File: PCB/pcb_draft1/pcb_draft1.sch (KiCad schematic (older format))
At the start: 63 parts, among them Q1 DMN6140L, Q10 DMN6140L, Q11 DMN6140L, Q12 DMN6140L, Q13 DMN6140L, Q14 DMN6140L, Q15 DMN6140L, Q2 DMN6140L, Q3 DMN6140L, Q4 DMN6140L, Q5 DMN6140L, Q6 DMN6140L, Q7 DMN6140L, Q8 DMN6140L, Q9 DMN6140L, U1 STSPIN820, U2 STSPIN820

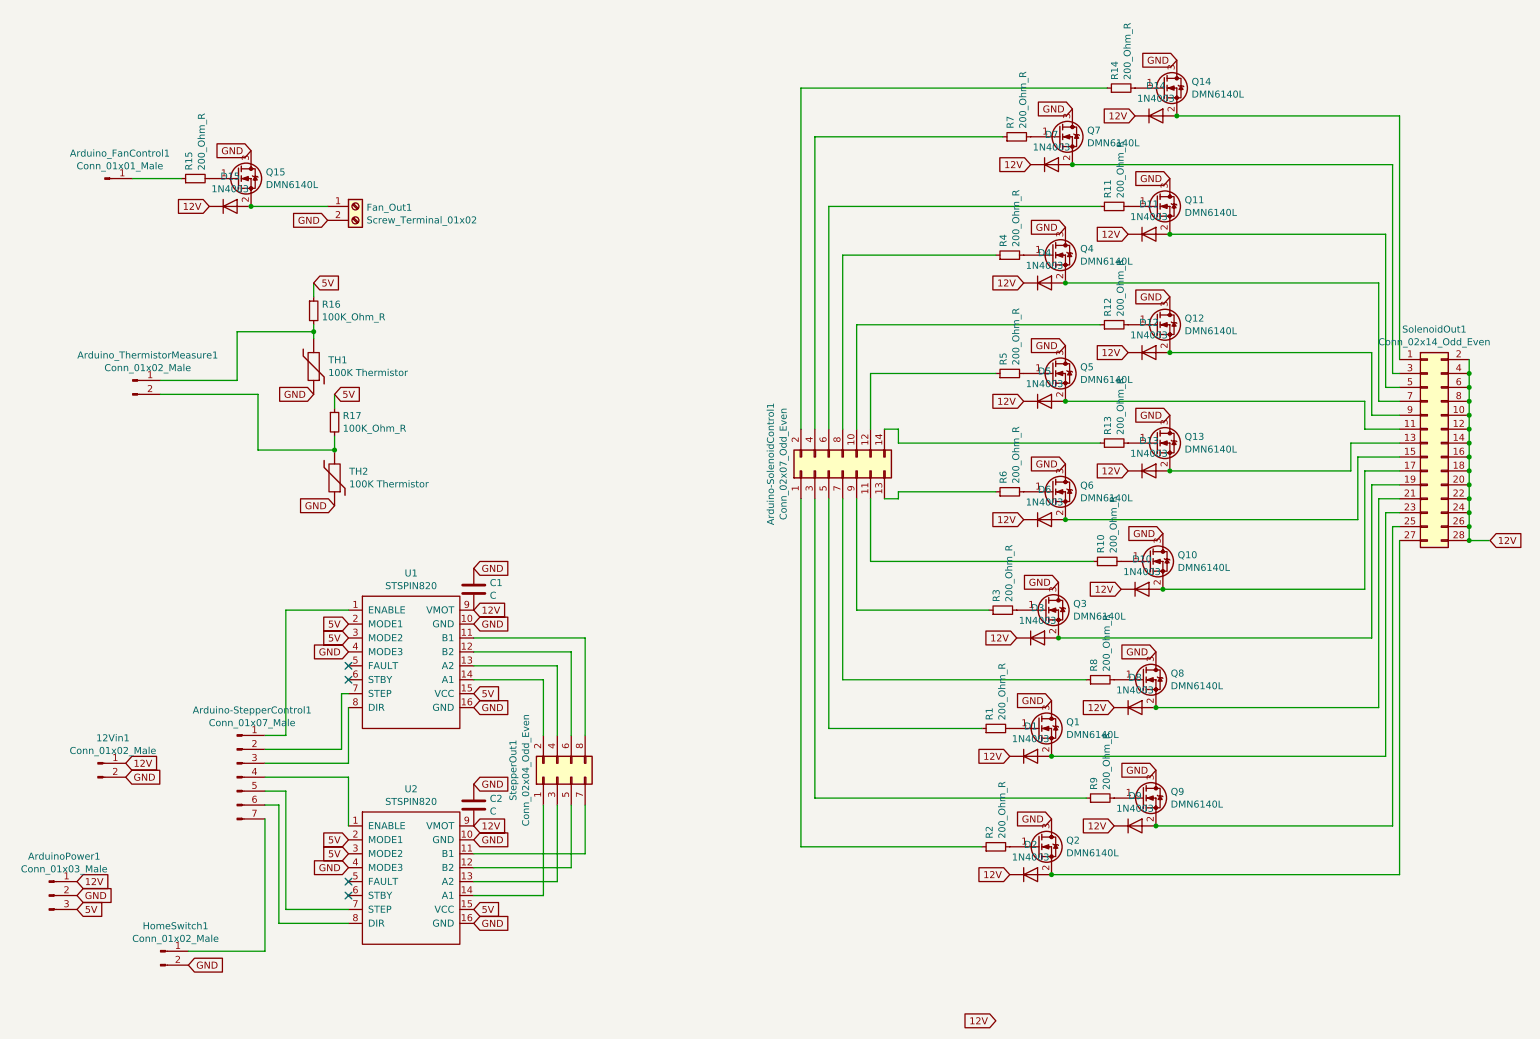
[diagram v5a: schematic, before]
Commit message: Update PCB with accurate connector types
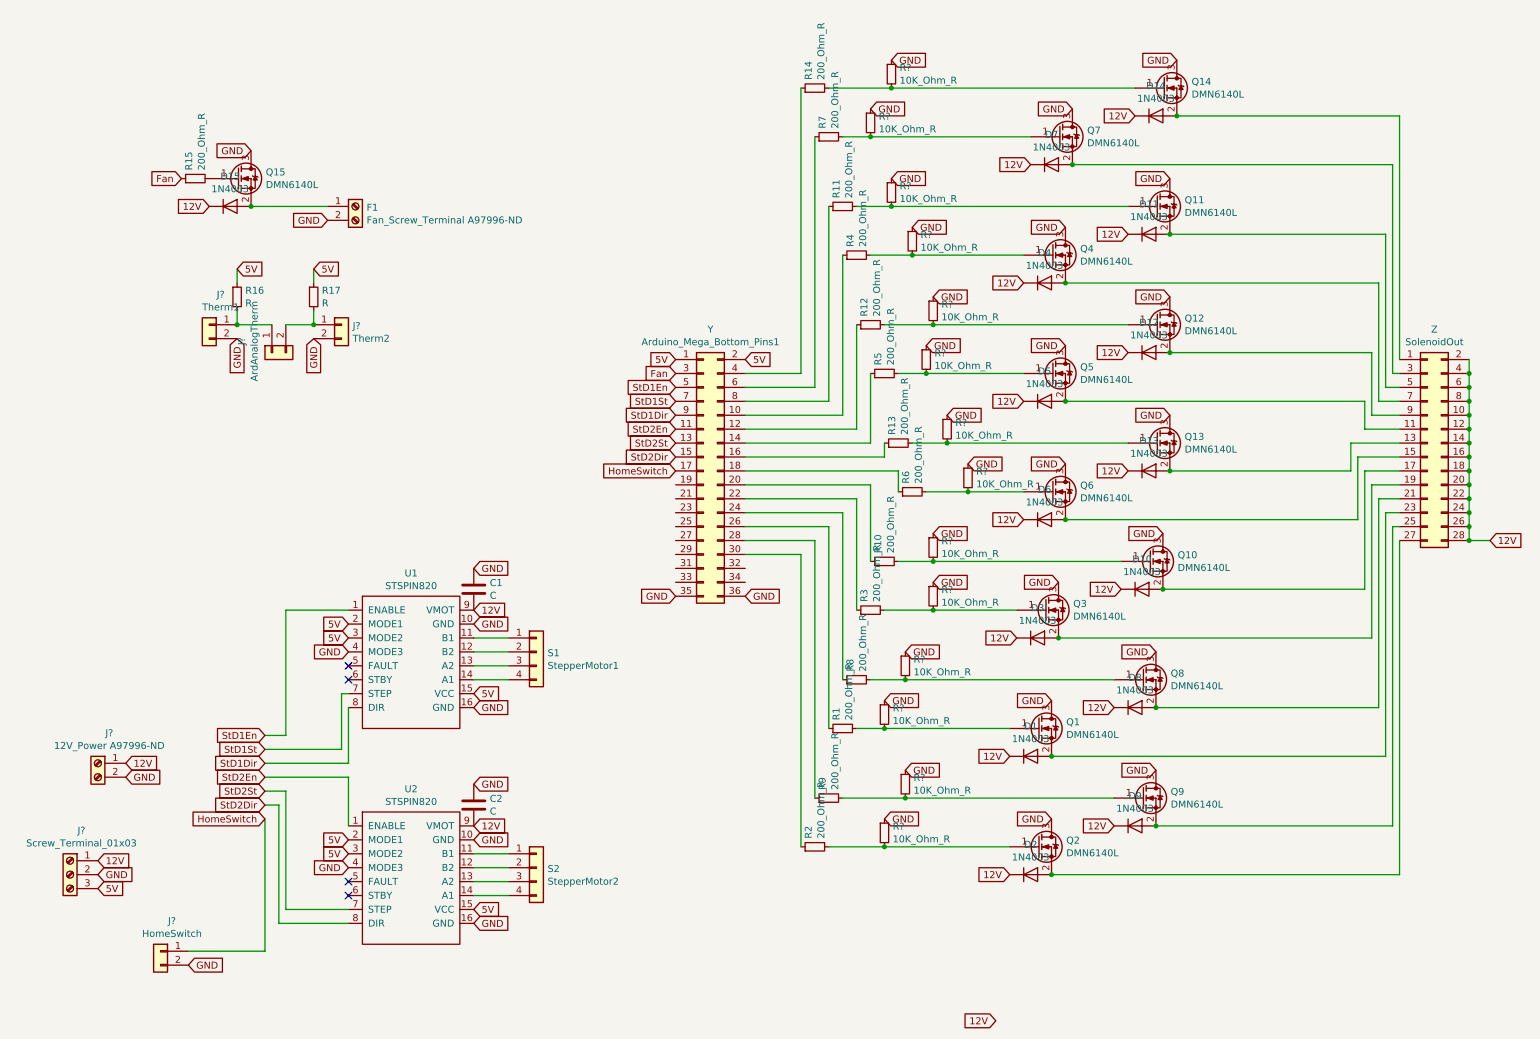
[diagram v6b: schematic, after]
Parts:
- removed 12Vin1, Arduino_ThermistorMeasure1, HomeSwitch1: Conn_01x02_Male, Connector_PinHeader_2.54mm:PinHeader_1x02_P2.54mm_Vertical, symbol Connector:Conn_01x02_Male
- removed Arduino-SolenoidControl1: Conn_02x07_Odd_Even, Connector_PinHeader_2.54mm:PinHeader_2x07_P2.54mm_Vertical, symbol Connector_Generic:Conn_02x07_Odd_Even
- removed Arduino-StepperControl1: Conn_01x07_Male, Connector_PinHeader_2.54mm:PinHeader_1x07_P2.54mm_Vertical, symbol Connector:Conn_01x07_Male
- removed ArduinoPower1: Conn_01x03_Male, Connector_PinHeader_2.54mm:PinHeader_1x03_P2.54mm_Vertical, symbol Connector:Conn_01x03_Male
- removed Arduino_FanControl1: Conn_01x01_Male, Connector_PinHeader_2.54mm:PinHeader_1x01_P2.54mm_Vertical, symbol Connector:Conn_01x01_Male
- removed StepperOut1: Conn_02x04_Odd_Even, Connector_PinHeader_2.54mm:PinHeader_2x04_P2.54mm_Vertical, symbol Connector_Generic:Conn_02x04_Odd_Even
- removed TH1, TH2: 100K Thermistor, symbol Device:Thermistor
- added J?: ArdAnalogTherm, symbol Connector_Generic:Conn_01x02
- added J?: Therm1, symbol Connector_Generic:Conn_01x02
- added J?: Therm2, symbol Connector_Generic:Conn_01x02
- added J?: HomeSwitch, symbol Connector_Generic:Conn_01x02
- added J?: Screw_Terminal_01x03, symbol Connector:Screw_Terminal_01x03
- added J?: 12V_Power A97996-ND, symbol Connector:Screw_Terminal_01x02
- added R? (x14): 10K_Ohm_R, symbol Device:R_Small
- added S1: StepperMotor1, symbol Connector_Generic:Conn_01x04
- added S2: StepperMotor2, symbol Connector_Generic:Conn_01x04
- added Y: Arduino_Mega_Bottom_Pins1, symbol Connector_Generic:Conn_02x18_Odd_Even
- F1: renamed from Fan_Out1; value Screw_Terminal_01x02 -> Fan_Screw_Terminal A97996-ND
- R16, R17: value 100K_Ohm_R -> R
- Z: renamed from SolenoidOut1; value Conn_02x14_Odd_Even -> SolenoidOut
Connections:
- net 12V: now also J?.1 (Pin_1), J?.1 (Pin_1)
- net 5V: now also J?.3 (Pin_3), Y.1 (Pin_1), Y.2 (Pin_2)
- net GND: now also J?.2 (Pin_2), J?.2 (Pin_2), J?.2 (Pin_2), J?.2 (Pin_2), J?.2 (Pin_2), R?.1, R?.1, R?.1, R?.1, R?.1, R?.1, R?.1, R?.1, R?.1, R?.1, R?.1, R?.1, R?.1, R?.1, Y.35 (Pin_35), Y.36 (Pin_36)
- net StD1En: now reaches U1.1 (ENABLE)
- net StD1En: now also Y.5 (Pin_5)
- net StD1St: now reaches U1.7 (STEP)
- net StD1St: now also Y.7 (Pin_7)
- net StD1Dir: now reaches U1.8 (DIR)
- net StD1Dir: now also Y.9 (Pin_9)
- net StD2En: now reaches U2.1 (ENABLE)
- net StD2En: now also Y.11 (Pin_11)
- net StD2St: now reaches U2.7 (STEP)
- net StD2St: now also Y.13 (Pin_13)
- net StD2Dir: now reaches U2.8 (DIR)
- net StD2Dir: now also Y.15 (Pin_15)
- net at Q14.1 (G), R14.2: now also R?.2
- net at R14.1: now also Y.4 (Pin_4)
- net at U2.11 (B1): now also S2.1 (Pin_1)
- net at U2.12 (B2): now also S2.2 (Pin_2)
- net at U2.13 (A2): now also S2.3 (Pin_3)
- net at U2.14 (A1): now also S2.4 (Pin_4)
- net at U1.11 (B1): now also S1.1 (Pin_1)
- net at U1.12 (B2): now also S1.2 (Pin_2)
- net at U1.13 (A2): now also S1.3 (Pin_3)
- net at U1.14 (A1): now also S1.4 (Pin_4)
- net at R7.1: now also Y.6 (Pin_6)
- net at Q7.1 (G), R7.2: now also R?.2
- net at R11.1: now also Y.8 (Pin_8)
- net at Q11.1 (G), R11.2: now also R?.2
- net at R4.1: now also Y.10 (Pin_10)
- net at Q4.1 (G), R4.2: now also R?.2
- net at R12.1: now also Y.12 (Pin_12)
- net at Q12.1 (G), R12.2: now also R?.2
- net at R5.1: now also Y.14 (Pin_14)
- net at Q5.1 (G), R5.2: now also R?.2
- net at R13.1: now also Y.16 (Pin_16)
- net at Q13.1 (G), R13.2: now also R?.2
- net at R6.1: now also Y.18 (Pin_18)
- net at Q6.1 (G), R6.2: now also R?.2
- net at R10.1: now also Y.20 (Pin_20)
- net at Q10.1 (G), R10.2: now also R?.2
- net at R3.1: now also Y.22 (Pin_22)
- net at Q3.1 (G), R3.2: now also R?.2
- net at R8.1: now also Y.24 (Pin_24)
- net at Q8.1 (G), R8.2: now also R?.2
- net at R1.1: now also Y.26 (Pin_26)
- net at Q1.1 (G), R1.2: now also R?.2
- net at R9.1: now also Y.28 (Pin_28)
- net at Q9.1 (G), R9.2: now also R?.2
- net at R2.1: now also Y.30 (Pin_30)
- net at Q2.1 (G), R2.2: now also R?.2
- net Fan: now reaches R15.1
- net Fan: now also Y.3 (Pin_3)
- net at R16.2: now also J?.1 (Pin_1), J?.1 (Pin_1)
- net at R17.2: now also J?.1 (Pin_1), J?.2 (Pin_2)
- new net HomeSwitch: J?.1 (Pin_1), Y.17 (Pin_17)
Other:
- moved on the sheet: R1, R10, R11, R12, R13, R14, R16, R17, R2, R3, R4, R5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

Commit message: add new netlist
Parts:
- gave numbers to parts that had none: 20
- renumbered Y to Y1, Z to Z1
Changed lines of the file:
@@
 GND
 $Comp
-L Connector_Generic:Conn_02x14_Odd_Even Z
+L Connector_Generic:Conn_02x14_Odd_Even Z1
 U 1 1 5DE02A66
 P 10650 3350
-F 0 "Z" H 10700 4167 50  0000 C CNN
+F 0 "Z1" H 10700 4167 50  0000 C CNN
 F 1 "SolenoidOut" H 10700 4076 50  0000 C CNN
 F 2 "Connector_PinHeader_2.54mm:PinHeader_2x14_P2.54mm_Vertical" H 10650 3350 50  0001 C CNN
@@
 $EndComp
 $Comp
-L Connector_Generic:Conn_02x18_Odd_Even Y
+L Connector_Generic:Conn_02x18_Odd_Even Y1
 U 1 1 5DC92377
 P 5450 3550
-F 0 "Y" H 5500 4567 50  0000 C CNN
+F 0 "Y1" H 5500 4567 50  0000 C CNN
 F 1 "Arduino_Mega_Bottom_Pins1" H 5500 4476 50  0000 C CNN
 F 2 "" H 5450 3550 50  0001 C CNN
@@
 	6450 1150 6650 1150
 $Comp
-L Device:R_Small R?
+L Device:R_Small R21
 U 1 1 5DF601F7
 P 6800 700
-F 0 "R?" H 6859 746 50  0000 L CNN
+F 0 "R21" H 6859 746 50  0000 L CNN
 F 1 "10K_Ohm_R" H 6859 655 50  0000 L CNN
 F 2 "" H 6800 700 50  0001 C CNN
@@
 GND
 $Comp
-L Device:R_Small R?
+L Device:R_Small R18
 U 1 1 5DF835D5
 P 6650 1050
-F 0 "R?" H 6709 1096 50  0000 L CNN
+F 0 "R18" H 6709 1096 50  0000 L CNN
 F 1 "10K_Ohm_R" H 6709 1005 50  0000 L CNN
 F 2 "" H 6650 1050 50  0001 C CNN
@@
 GND
 $Comp
-L Device:R_Small R?
+L Device:R_Small R22
 U 1 1 5DF8D93D
 P 6800 1550
-F 0 "R?" H 6859 1596 50  0000 L CNN
+F 0 "R22" H 6859 1596 50  0000 L CNN
 F 1 "10K_Ohm_R" H 6859 1505 50  0000 L CNN
 F 2 "" H 6800 1550 50  0001 C CNN
@@
 GND
 $Comp
-L Device:R_Small R?
+L Device:R_Small R25
 U 1 1 5DF994C1
 P 6950 1900
-F 0 "R?" H 7009 1946 50  0000 L CNN
+F 0 "R25" H 7009 1946 50  0000 L CNN
 F 1 "10K_Ohm_R" H 7009 1855 50  0000 L CNN
 F 2 "" H 6950 1900 50  0001 C CNN
@@
 GND
 $Comp
-L Device:R_Small R?
+L Device:R_Small R27
 U 1 1 5DFA4085
 P 7100 2400
-F 0 "R?" H 7159 2446 50  0000 L CNN
+F 0 "R27" H 7159 2446 50  0000 L CNN
 F 1 "10K_Ohm_R" H 7159 2355 50  0000 L CNN
 F 2 "" H 7100 2400 50  0001 C CNN
@@
 GND
 $Comp
-L Device:R_Small R?
+L Device:R_Small R26
 U 1 1 5DFAF044
 P 7050 2750
-F 0 "R?" H 7109 2796 50  0000 L CNN
+F 0 "R26" H 7109 2796 50  0000 L CNN
 F 1 "10K_Ohm_R" H 7109 2705 50  0000 L CNN
 F 2 "" H 7050 2750 50  0001 C CNN
@@
 GND
 $Comp
-L Device:R_Small R?
+L Device:R_Small R30
 U 1 1 5DFBB4AE
 P 7200 3250
-F 0 "R?" H 7259 3296 50  0000 L CNN
+F 0 "R30" H 7259 3296 50  0000 L CNN
 F 1 "10K_Ohm_R" H 7259 3205 50  0000 L CNN
 F 2 "" H 7200 3250 50  0001 C CNN
@@
 GND
 $Comp
-L Device:R_Small R?
+L Device:R_Small R31
 U 1 1 5DFC291D
 P 7350 3600
-F 0 "R?" H 7409 3646 50  0000 L CNN
+F 0 "R31" H 7409 3646 50  0000 L CNN
 F 1 "10K_Ohm_R" H 7409 3555 50  0000 L CNN
 F 2 "" H 7350 3600 50  0001 C CNN
@@
 GND
 $Comp
-L Device:R_Small R?
+L Device:R_Small R28
 U 1 1 5DFD5CE2
 P 7100 4100
-F 0 "R?" H 7159 4146 50  0000 L CNN
+F 0 "R28" H 7159 4146 50  0000 L CNN
 F 1 "10K_Ohm_R" H 7159 4055 50  0000 L CNN
 F 2 "" H 7100 4100 50  0001 C CNN
@@
 GND
 $Comp
-L Device:R_Small R?
+L Device:R_Small R29
 U 1 1 5DFE1F17
 P 7100 4450
-F 0 "R?" H 7159 4496 50  0000 L CNN
+F 0 "R29" H 7159 4496 50  0000 L CNN
 F 1 "10K_Ohm_R" H 7159 4405 50  0000 L CNN
 F 2 "" H 7100 4450 50  0001 C CNN
@@
 GND
 $Comp
-L Device:R_Small R?
+L Device:R_Small R23
 U 1 1 5DFEE488
 P 6900 4950
-F 0 "R?" H 6959 4996 50  0000 L CNN
+F 0 "R23" H 6959 4996 50  0000 L CNN
 F 1 "10K_Ohm_R" H 6959 4905 50  0000 L CNN
 F 2 "" H 6900 4950 50  0001 C CNN
@@
 GND
 $Comp
-L Device:R_Small R?
+L Device:R_Small R19
 U 1 1 5DFFB192
 P 6750 5300
-F 0 "R?" H 6809 5346 50  0000 L CNN
+F 0 "R19" H 6809 5346 50  0000 L CNN
 F 1 "10K_Ohm_R" H 6809 5255 50  0000 L CNN
 F 2 "" H 6750 5300 50  0001 C CNN
@@
 GND
 $Comp
-L Device:R_Small R?
+L Device:R_Small R24
 U 1 1 5E008535
 P 6900 5800
-F 0 "R?" H 6959 5846 50  0000 L CNN
+F 0 "R24" H 6959 5846 50  0000 L CNN
 F 1 "10K_Ohm_R" H 6959 5755 50  0000 L CNN
 F 2 "" H 6900 5800 50  0001 C CNN
@@
 GND
 $Comp
-L Device:R_Small R?
+L Device:R_Small R20
 U 1 1 5E015A54
 P 6750 6150
-F 0 "R?" H 6809 6196 50  0000 L CNN
+F 0 "R20" H 6809 6196 50  0000 L CNN
 F 1 "10K_Ohm_R" H 6809 6105 50  0000 L CNN
 F 2 "" H 6750 6150 50  0001 C CNN
@@
 	6750 6250 7650 6250
 $Comp
-L Connector_Generic:Conn_01x02 J?
+L Connector_Generic:Conn_01x02 J5
 U 1 1 5E032CCA
 P 2350 2700
-F 0 "J?" H 2268 2917 50  0000 C CNN
+F 0 "J5" H 2268 2917 50  0000 C CNN
 F 1 "ArdAnalogTherm" H 2268 2826 50  0000 C CNN
 F 2 "" H 2350 2700 50  0001 C CNN
@@
 	2100 2400 2100 2500
 $Comp
-L Connector_Generic:Conn_01x02 J?
+L Connector_Generic:Conn_01x02 J4
 U 1 1 5E0A79D3
 P 1900 2500
-F 0 "J?" H 1818 2717 50  0000 C CNN
+F 0 "J4" H 1818 2717 50  0000 C CNN
 F 1 "Therm1" H 1818 2626 50  0000 C CNN
 F 2 "" H 1900 2500 50  0001 C CNN
@@
 $EndComp
 $Comp
-L Connector_Generic:Conn_01x02 J?
+L Connector_Generic:Conn_01x02 J6
 U 1 1 5E0F6803
 P 2850 2500
-F 0 "J?" H 2930 2492 50  0000 L CNN
+F 0 "J6" H 2930 2492 50  0000 L CNN
 F 1 "Therm2" H 2930 2401 50  0000 L CNN
 F 2 "" H 2850 2500 50  0001 C CNN
@@
 GND
 $Comp
-L Connector_Generic:Conn_01x02 J?
+L Connector_Generic:Conn_01x02 J3
 U 1 1 5E141524
 P 1550 7000
-F 0 "J?" H 1468 7217 50  0000 C CNN
+F 0 "J3" H 1468 7217 50  0000 C CNN
 F 1 "HomeSwitch" H 1468 7126 50  0000 C CNN
 F 2 "" H 1550 7000 50  0001 C CNN
@@
 $EndComp
 $Comp
-L Connector:Screw_Terminal_01x03 J?
+L Connector:Screw_Terminal_01x03 J1
 U 1 1 5E155D7D
 P 900 6450
-F 0 "J?" H 818 6767 50  0000 C CNN
+F 0 "J1" H 818 6767 50  0000 C CNN
 F 1 "Screw_Terminal_01x03" H 818 6676 50  0000 C CNN
 F 2 "" H 900 6450 50  0001 C CNN
@@
 $EndComp
 $Comp
-L Connector:Screw_Terminal_01x02 J?
+L Connector:Screw_Terminal_01x02 J2
 U 1 1 5E15FADE
 P 1100 5650
-F 0 "J?" H 1018 5867 50  0000 C CNN
+F 0 "J2" H 1018 5867 50  0000 C CNN
 F 1 "12V_Power A97996-ND " H 1018 5776 50  0000 C CNN
 F 2 "" H 1100 5650 50  0001 C CNN
